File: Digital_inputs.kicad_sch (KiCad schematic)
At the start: 21 parts, among them U2 ISO1212, U3 ISO1212

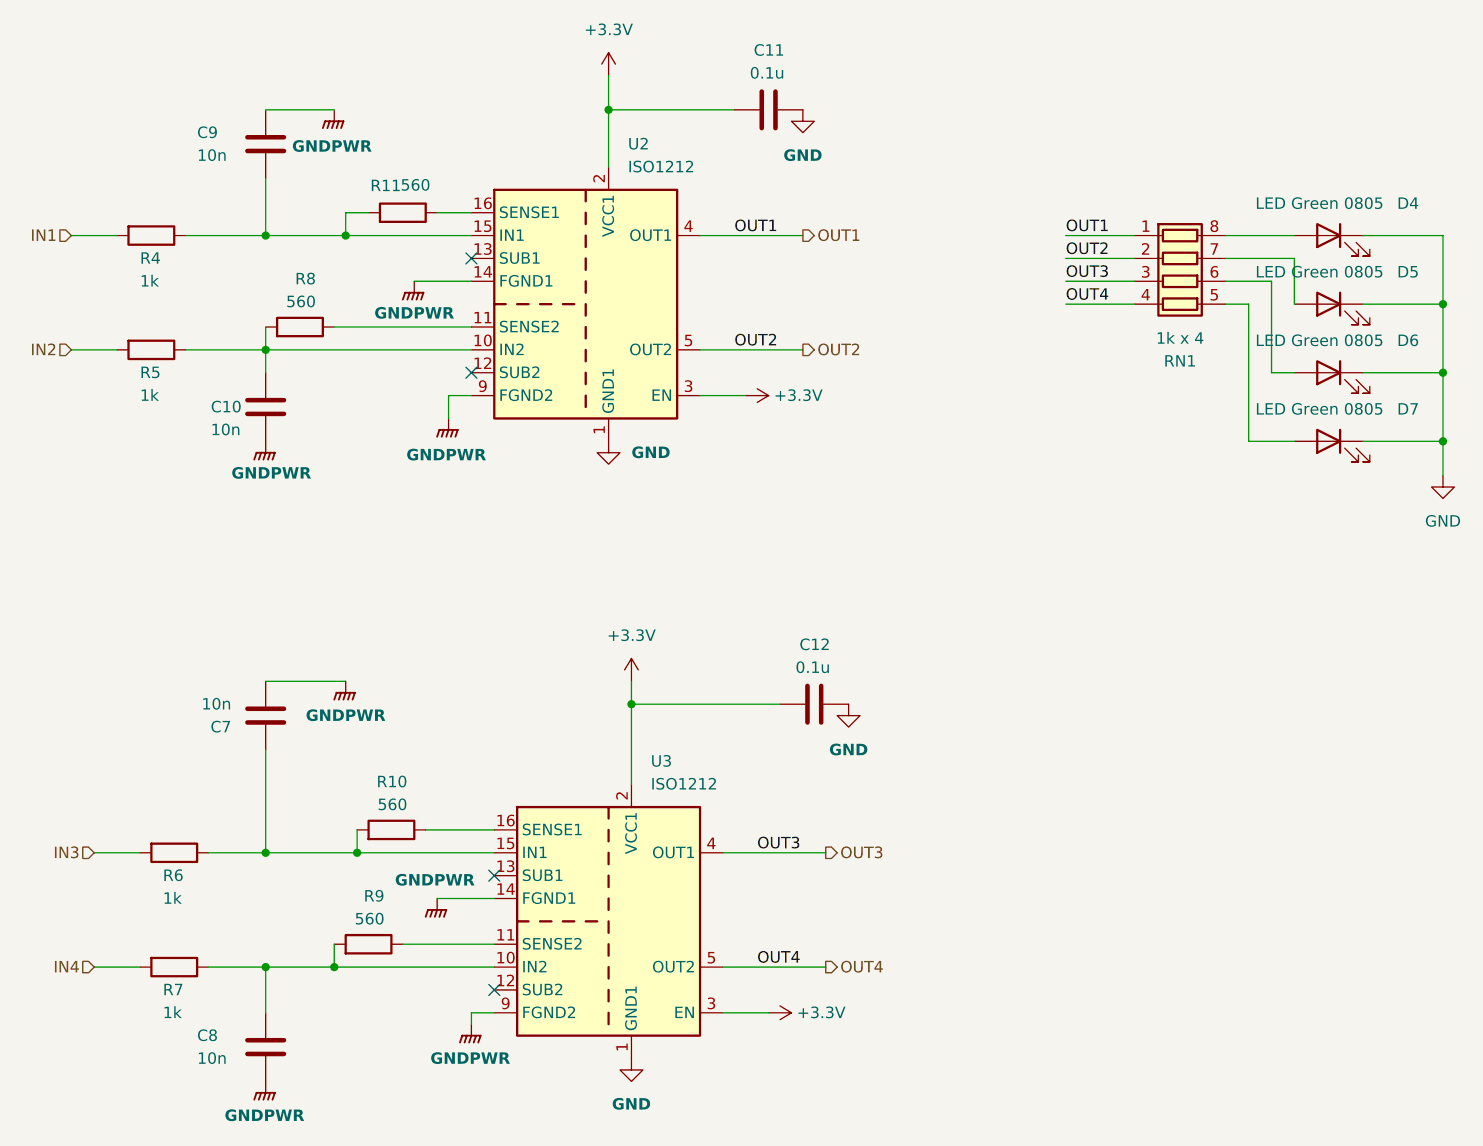
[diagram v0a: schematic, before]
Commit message: Трассировка питания и цифровых входов-выходов
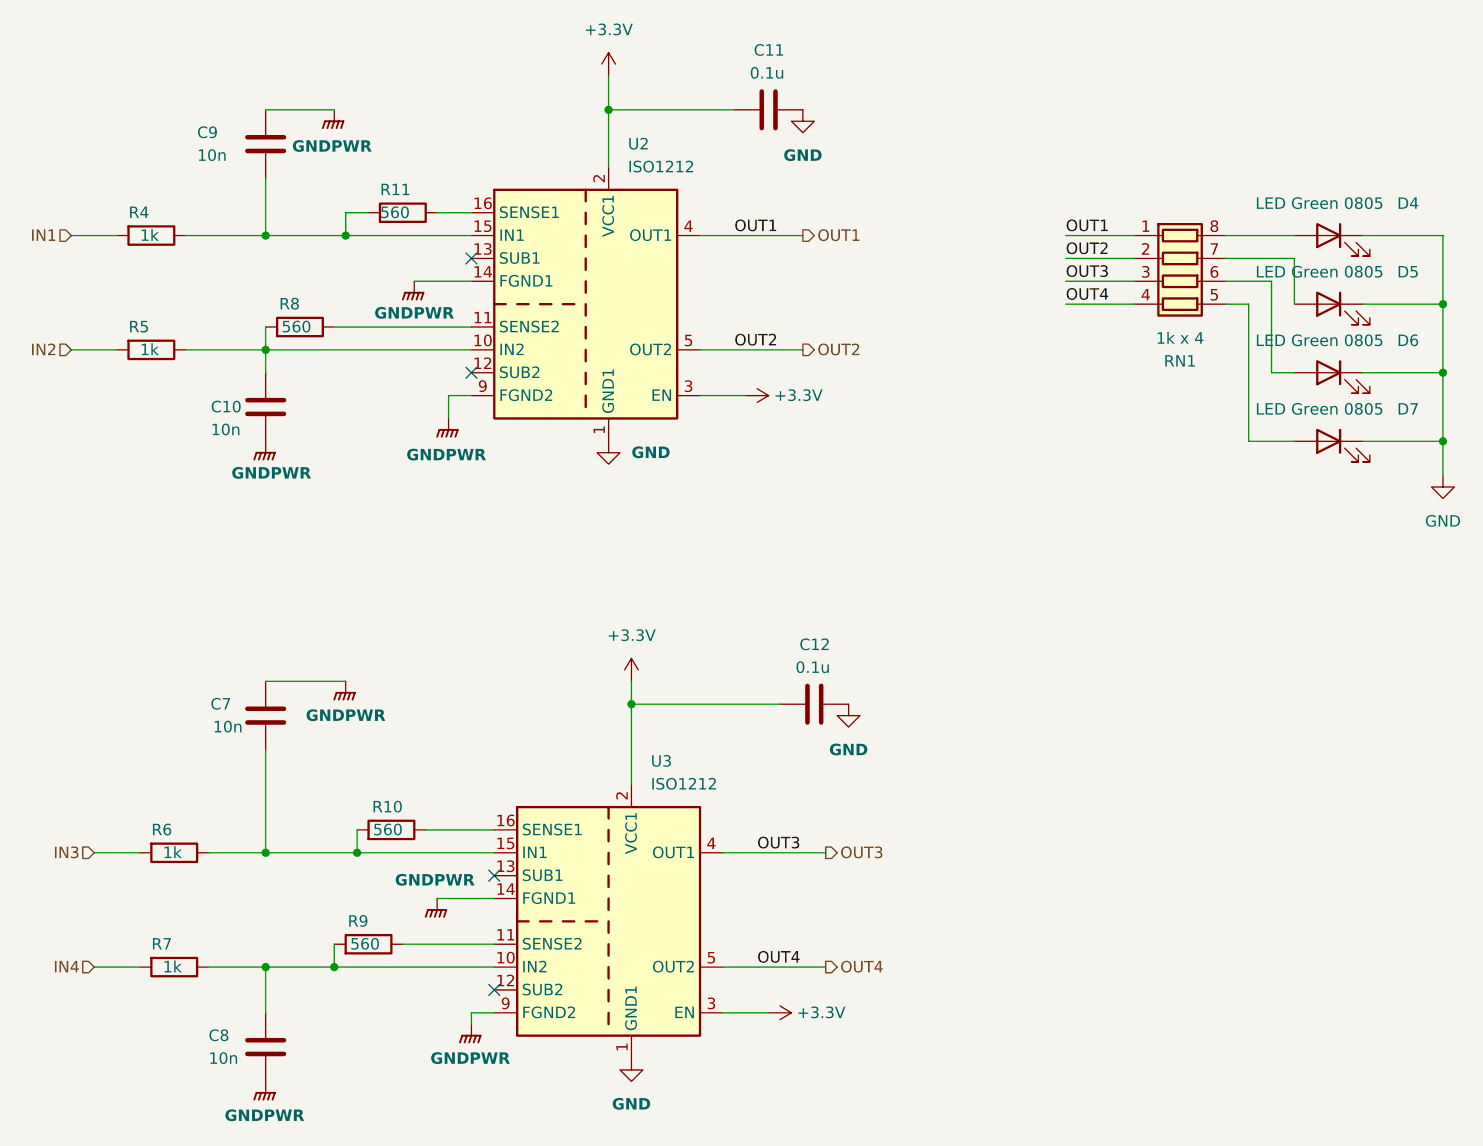
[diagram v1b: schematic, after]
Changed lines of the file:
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@@
 		(dnp no)
 		(property "Reference" "C7"
-			(at 90.17 107.95 0)
+			(at 90.17 105.41 0)
 			(show_name no)
 			(do_not_autoplace no)
@@
 		)
 		(property "Value" "10n"
-			(at 90.17 105.41 0)
+			(at 91.44 107.95 0)
 			(show_name no)
 			(do_not_autoplace yes)
@@
 		(dnp no)
 		(property "Reference" "R7"
-			(at 82.55 137.1599 90)
+			(at 81.28 132.08 90)
 			(show_name no)
 			(do_not_autoplace yes)
@@
 		)
 		(property "Value" "1k"
-			(at 82.55 139.6999 90)
+			(at 82.55 134.62 90)
 			(show_name no)
 			(do_not_autoplace no)
@@
 		(dnp no)
 		(property "Reference" "R6"
-			(at 82.55 124.4599 90)
+			(at 81.28 119.38 90)
 			(show_name no)
 			(do_not_autoplace yes)
@@
 		)
 		(property "Value" "1k"
-			(at 82.55 126.9999 90)
+			(at 82.55 121.92 90)
 			(show_name no)
 			(do_not_autoplace no)
@@
 		(dnp no)
 		(property "Reference" "R8"
-			(at 99.568 58.166 90)
+			(at 97.79 60.96 90)
 			(show_name no)
 			(do_not_autoplace yes)
@@
 		)
 		(property "Value" "560"
-			(at 99.568 60.706 90)
+			(at 99.06 63.5 90)
 			(show_name no)
 			(do_not_autoplace yes)
@@
 		(dnp no)
 		(property "Reference" "R5"
-			(at 80.01 68.5799 90)
+			(at 78.74 63.5 90)
 			(show_name no)
 			(do_not_autoplace yes)
@@
 		)
 		(property "Value" "1k"
-			(at 80.01 71.1199 90)
+			(at 80.01 66.04 90)
 			(show_name no)
 			(do_not_autoplace no)
@@
 		(dnp no)
 		(property "Reference" "R11"
-			(at 105.6005 47.8155 90)
+			(at 106.68 48.26 90)
 			(show_name no)
 			(do_not_autoplace yes)
@@
 		)
 		(property "Value" "560"
-			(at 108.966 47.752 90)
+			(at 106.68 50.8 90)
 			(show_name no)
 			(do_not_autoplace yes)
@@
 		(dnp no)
 		(property "Reference" "R9"
-			(at 107.188 126.746 90)
+			(at 105.41 129.54 90)
 			(show_name no)
 			(do_not_autoplace yes)
@@
 		)
 		(property "Value" "560"
-			(at 107.188 129.286 90)
+			(at 106.68 132.08 90)
 			(show_name no)
 			(do_not_autoplace yes)
@@
 		(dnp no)
 		(property "Reference" "R10"
-			(at 109.728 114.046 90)
+			(at 109.22 116.84 90)
 			(show_name no)
 			(do_not_autoplace yes)
@@
 		)
 		(property "Value" "560"
-			(at 109.728 116.586 90)
+			(at 109.22 119.38 90)
 			(show_name no)
 			(do_not_autoplace yes)
@@
 		(dnp no)
 		(property "Reference" "R4"
-			(at 80.01 55.8799 90)
+			(at 78.74 50.8 90)
 			(show_name no)
 			(do_not_autoplace yes)
@@
 		)
 		(property "Value" "1k"
-			(at 80.01 58.4199 90)
+			(at 80.01 53.34 90)
 			(show_name no)
 			(do_not_autoplace no)
@@
 		(dnp no)
 		(property "Reference" "C8"
-			(at 86.36 142.2399 0)
+			(at 87.63 142.24 0)
 			(show_name no)
 			(do_not_autoplace no)
@@
 		)
 		(property "Value" "10n"
-			(at 86.36 144.7799 0)
+			(at 87.63 144.78 0)
 			(show_name no)
 			(do_not_autoplace yes)
